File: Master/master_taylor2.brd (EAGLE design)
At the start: 54.1 x 51.3 mm, 51 parts, among them J1 ISP, U1 ATMEGA128RFA1, U2 TPS73633-DBVT, U3 ULN2003ADR, Y1 16MHz

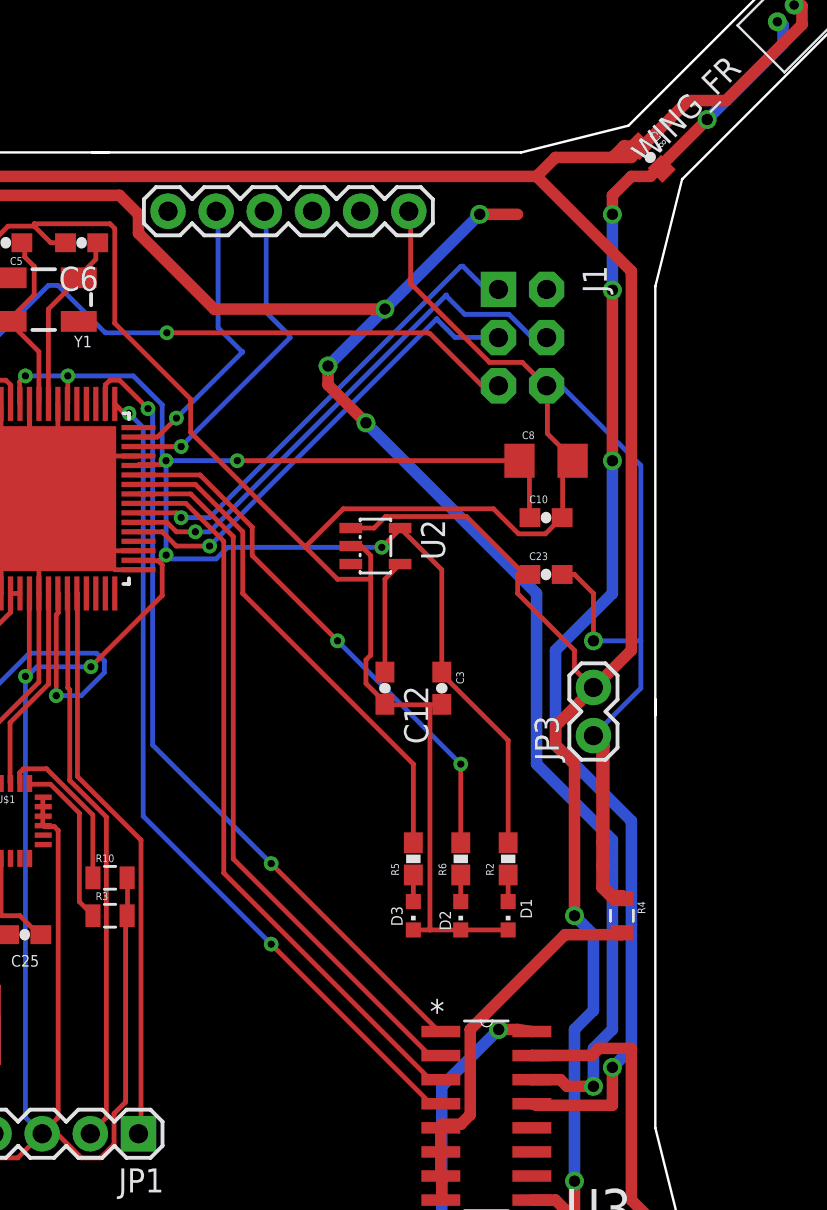
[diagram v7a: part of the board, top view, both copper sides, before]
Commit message: Spaced out headers a bit
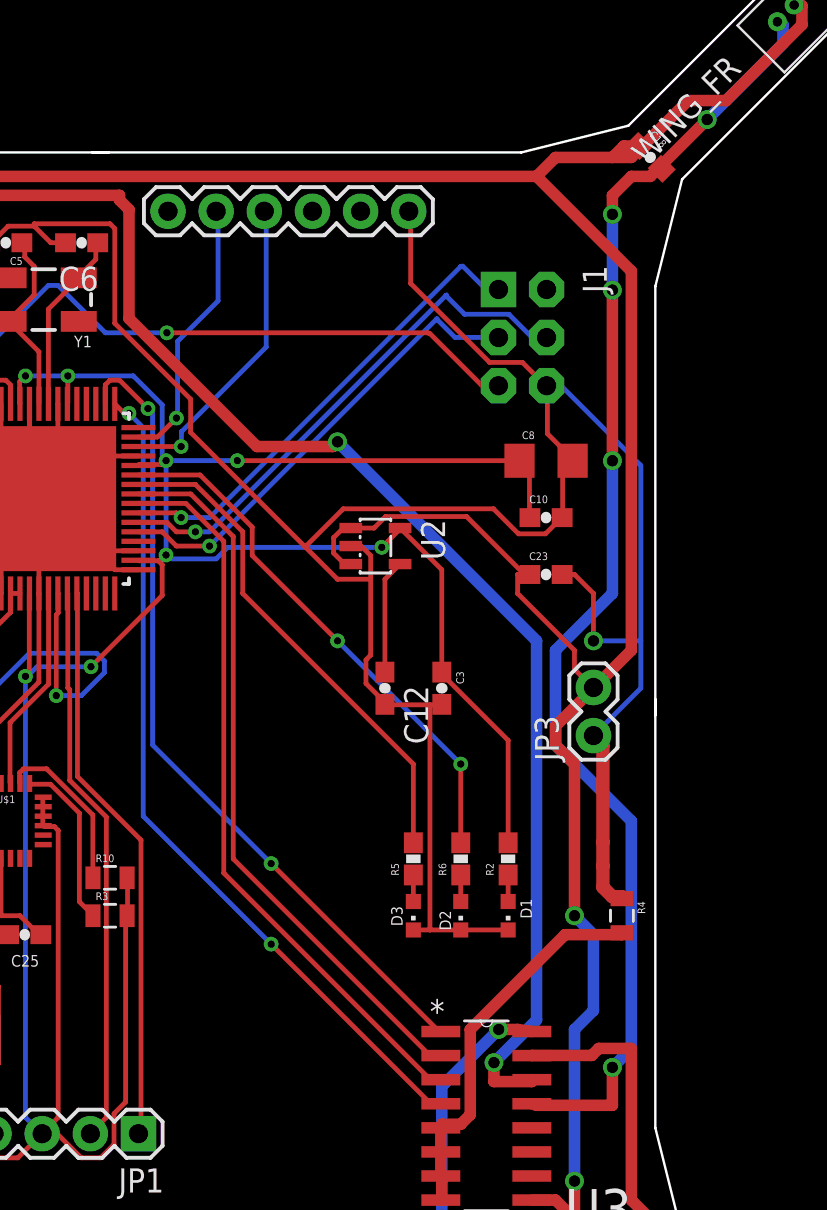
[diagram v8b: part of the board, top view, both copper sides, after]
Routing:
- net N$31: track 119.7 -> 103.0 mm, vias 5 -> 2
- net VBAT: track 252.3 -> 255.3 mm
- net TX0: track 15.4 -> 14.4 mm
- net RX0: track 17.6 -> 16.7 mm
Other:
- board text added: "Changes: -Reduced area to save weight -Keepout underneath IMU based on official recommendation -Most parts are 0603 for compactness -Better placement on crystal and antenna -Wings are made for 7mm motors -Removed useless parts -Moved connectors to match wire length -Spaced out ISP and FTDI headers"
- board text removed: "Changes: -Reduced area to save weight -Keepout underneath IMU based on official recommendation -Most parts are 0603 for compactness -Better placement on crystal and antenna -Wings are made for 7mm motors -Removed useless parts -Moved connectors to match wire length"
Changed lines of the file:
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@@
 -Wings are made for 7mm motors
 -Removed useless parts
--Moved connectors to match wire length</text>
+-Moved connectors to match wire length
+-Spaced out ISP and FTDI headers</text>
 </plain>
 <attributes>
@@
 <wire x1="3" y1="14.25" x2="2" y2="14.25" width="0.254" layer="1"/>
 <wire x1="4" y1="15.25" x2="3" y2="14.25" width="0.254" layer="1"/>
-<wire x1="7.5" y1="18.75" x2="7.4814" y2="18.7314" width="0.254" layer="16"/>
 <via x="4" y="15.25" extent="1-16" drill="0.381"/>
-<wire x1="7.4814" y1="18.7314" x2="4" y2="15.25" width="0.254" layer="16"/>
-<wire x1="6.1976" y1="20.0152" x2="6.1976" y2="26.1112" width="0.254" layer="16"/>
-<wire x1="7.4814" y1="18.7314" x2="6.1976" y2="20.0152" width="0.254" layer="16"/>
 <wire x1="6.1976" y1="26.1112" x2="6.098" y2="26.161" width="0.254" layer="16"/>
+<wire x1="4.064" y1="19.304" x2="4.064" y2="15.3416" width="0.254" layer="16"/>
+<wire x1="6.1976" y1="21.4376" x2="4.064" y2="19.304" width="0.254" layer="16"/>
+<wire x1="6.1976" y1="26.0096" x2="6.1976" y2="21.4376" width="0.254" layer="16"/>
+<wire x1="4.064" y1="15.3416" x2="4" y2="15.25" width="0.254" layer="16"/>
+<wire x1="6.1976" y1="26.0096" x2="6.098" y2="26.161" width="0.254" layer="16"/>
 </signal>
 <signal name="RX0">
@@
 <contactref element="JP9" pad="TXO"/>
 <wire x1="4.25" y1="13.75" x2="2" y2="13.75" width="0.254" layer="1"/>
-<wire x1="10" y1="19.5" x2="4.25" y2="13.75" width="0.254" layer="16"/>
 <via x="4.25" y="13.75" extent="1-16" drill="0.381"/>
-<wire x1="8.7376" y1="20.828" x2="8.7376" y2="26.1112" width="0.254" layer="16"/>
-<wire x1="9.9568" y1="19.6088" x2="8.7376" y2="20.828" width="0.254" layer="16"/>
 <wire x1="8.7376" y1="26.1112" x2="8.638" y2="26.161" width="0.254" layer="16"/>
-<wire x1="9.9568" y1="19.6088" x2="10" y2="19.5" width="0.254" layer="16"/>
+<wire x1="4.2672" y1="14.5288" x2="4.2672" y2="13.8176" width="0.254" layer="16"/>
+<wire x1="8.7376" y1="18.9992" x2="4.2672" y2="14.5288" width="0.254" layer="16"/>
+<wire x1="8.7376" y1="26.0096" x2="8.7376" y2="18.9992" width="0.254" layer="16"/>
+<wire x1="4.2672" y1="13.8176" x2="4.25" y2="13.75" width="0.254" layer="16"/>
+<wire x1="8.7376" y1="26.0096" x2="8.638" y2="26.161" width="0.254" layer="16"/>
 </signal>
 <signal name="TX1">
@@
 <wire x1="-31" y1="30" x2="-29.601040625" y2="28.601040625" width="0.6096" layer="1"/>
 <wire x1="-29.601040625" y1="28.601040625" x2="-29.601040625" y2="28.39895625" width="0.6096" layer="1"/>
-<wire x1="20" y1="26" x2="22" y2="26" width="0.6096" layer="1"/>
-<wire x1="15" y1="21" x2="20" y2="26" width="0.6096" layer="16"/>
-<wire x1="6" y1="21" x2="15" y2="21" width="0.6096" layer="1"/>
-<wire x1="2" y1="25" x2="6" y2="21" width="0.6096" layer="1"/>
-<wire x1="2" y1="26" x2="2" y2="25" width="0.6096" layer="1"/>
-<wire x1="1" y1="27" x2="2" y2="26" width="0.6096" layer="1"/>
 <wire x1="-28" y1="27" x2="1" y2="27" width="0.6096" layer="1"/>
 <wire x1="-29.601040625" y1="28.601040625" x2="-28" y2="27" width="0.6096" layer="1"/>
-<via x="20" y="26" extent="1-16" drill="0.6"/>
-<via x="15" y="21" extent="1-16" drill="0.6"/>
-<wire x1="26" y1="-20" x2="24.611" y2="-20" width="0.6096" layer="1"/>
-<wire x1="26" y1="-18" x2="26" y2="-20" width="0.6096" layer="16"/>
-<wire x1="27" y1="-17" x2="26" y2="-18" width="0.6096" layer="16"/>
-<wire x1="27" y1="-7" x2="27" y2="-17" width="0.6096" layer="16"/>
-<wire x1="23" y1="-3" x2="27" y2="-7" width="0.6096" layer="16"/>
-<wire x1="23" y1="6" x2="23" y2="-3" width="0.6096" layer="16"/>
-<wire x1="14" y1="15" x2="23" y2="6" width="0.6096" layer="16"/>
-<wire x1="12" y1="17" x2="14" y2="15" width="0.6096" layer="1"/>
-<wire x1="12" y1="18" x2="12" y2="17" width="0.6096" layer="1"/>
-<wire x1="15" y1="21" x2="12" y2="18" width="0.6096" layer="16"/>
-<via x="26" y="-20" extent="1-16" drill="0.6"/>
-<via x="14" y="15" extent="1-16" drill="0.6"/>
-<via x="12" y="18" extent="1-16" drill="0.6"/>
-<wire x1="24.611" y1="-20" x2="24.26" y2="-19.649" width="0.6096" layer="1"/>
-<wire x1="24.26" y1="-19.649" x2="22.751" y2="-19.649" width="0.6096" layer="1"/>
-<wire x1="22.751" y1="-19.649" x2="22.75" y2="-19.65" width="0.6096" layer="1"/>
+<wire x1="20.75" y1="-18.75" x2="20.75" y2="-19.75" width="0.6096" layer="1"/>
+<wire x1="23" y1="-16.5" x2="20.75" y2="-18.75" width="0.6096" layer="16"/>
+<wire x1="23" y1="3.5" x2="23" y2="-16.5" width="0.6096" layer="16"/>
+<wire x1="12.5" y1="14" x2="23" y2="3.5" width="0.6096" layer="16"/>
+<wire x1="12.25" y1="13.75" x2="12.5" y2="14" width="0.6096" layer="1"/>
+<wire x1="8.25" y1="13.75" x2="12.25" y2="13.75" width="0.6096" layer="1"/>
+<wire x1="1.5" y1="20.5" x2="8.25" y2="13.75" width="0.6096" layer="1"/>
+<wire x1="1.5" y1="26.25" x2="1.5" y2="20.5" width="0.6096" layer="1"/>
+<wire x1="1" y1="26.75" x2="1.5" y2="26.25" width="0.6096" layer="1"/>
+<wire x1="1" y1="26.75" x2="1" y2="27" width="0.6096" layer="1"/>
+<wire x1="22.75" y1="-19.75" x2="20.75" y2="-19.75" width="0.6096" layer="1"/>
+<wire x1="22.75" y1="-19.75" x2="22.75" y2="-19.65" width="0.6096" layer="1"/>
+<via x="20.75" y="-18.75" extent="1-16" drill="0.6"/>
+<via x="12.5" y="14" extent="1-16" drill="0.6"/>
 </signal>
 <signal name="N$32">
@@
 <wire x1="36" y1="36" x2="35.70305625" y2="36.15605625" width="0.6096" layer="16"/>
 <via x="32" y="31" extent="1-16" drill="0.6"/>
-<wire x1="32" y1="31" x2="30" y2="29" width="0.6096" layer="1"/>
-<wire x1="30" y1="29" x2="29.601040625" y2="28.601040625" width="0.6096" layer="1"/>
+<wire x1="32" y1="31" x2="29.601040625" y2="28.601040625" width="0.6096" layer="1"/>
 <wire x1="29.601040625" y1="28.601040625" x2="29.601040625" y2="28.39895625" width="0.6096" layer="1"/>
 <wire x1="27" y1="-19" x2="27" y2="-21" width="0.6096" layer="1"/>
@@
 <via x="-28" y="-22" extent="1-16" drill="0.6"/>
 <via x="-27" y="28" extent="1-16" drill="0.6"/>
-<wire x1="13.2" y1="7.55" x2="13.2" y2="9.45" width="0" layer="19" extent="1-1"/>
 <wire x1="-29.601040625" y1="-28.39895625" x2="-28" y2="-26.797915625" width="0.6096" layer="1"/>
 <wire x1="-28" y1="-26.797915625" x2="-28" y2="-22" width="0.6096" layer="1"/>
+<wire x1="12.8016" y1="7.62" x2="13.1064" y2="7.62" width="0.254" layer="1"/>
+<wire x1="12.2936" y1="8.128" x2="12.8016" y2="7.62" width="0.254" layer="1"/>
+<wire x1="12.2936" y1="8.9408" x2="12.2936" y2="8.128" width="0.254" layer="1"/>
+<wire x1="12.8016" y1="9.4488" x2="12.2936" y2="8.9408" width="0.254" layer="1"/>
+<wire x1="13.1064" y1="9.4488" x2="12.8016" y2="9.4488" width="0.254" layer="1"/>
+<wire x1="13.1064" y1="7.62" x2="13.2" y2="7.55" width="0.254" layer="1"/>
+<wire x1="13.1064" y1="9.4488" x2="13.2" y2="9.45" width="0.254" layer="1"/>
 </signal>
 <signal name="N$20">
